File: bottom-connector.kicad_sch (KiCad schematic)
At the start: 6 parts, among them J1 Compute-Module-4_Plug_Connect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, Q3 DZDH0401DW, Q9 AO3401A

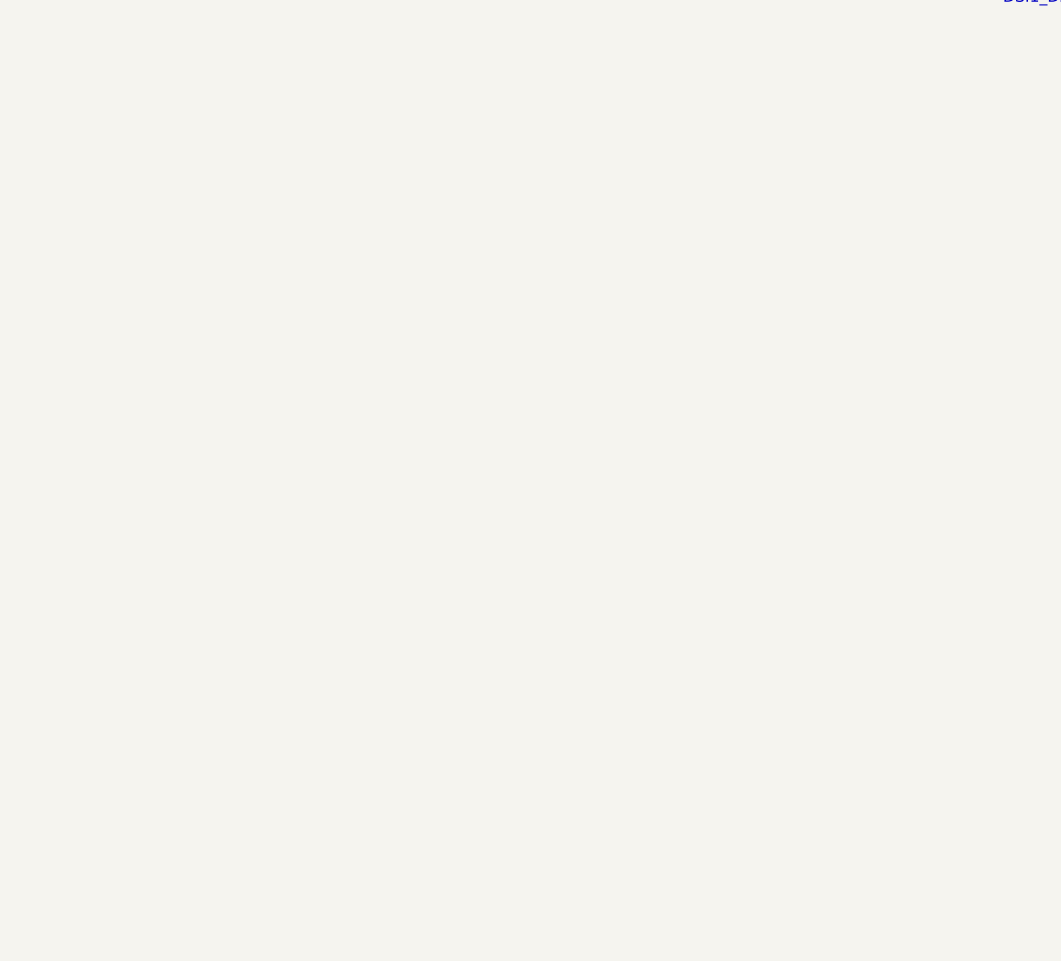
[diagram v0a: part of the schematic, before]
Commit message: [#57505] Continue migration to hierarchical schematic
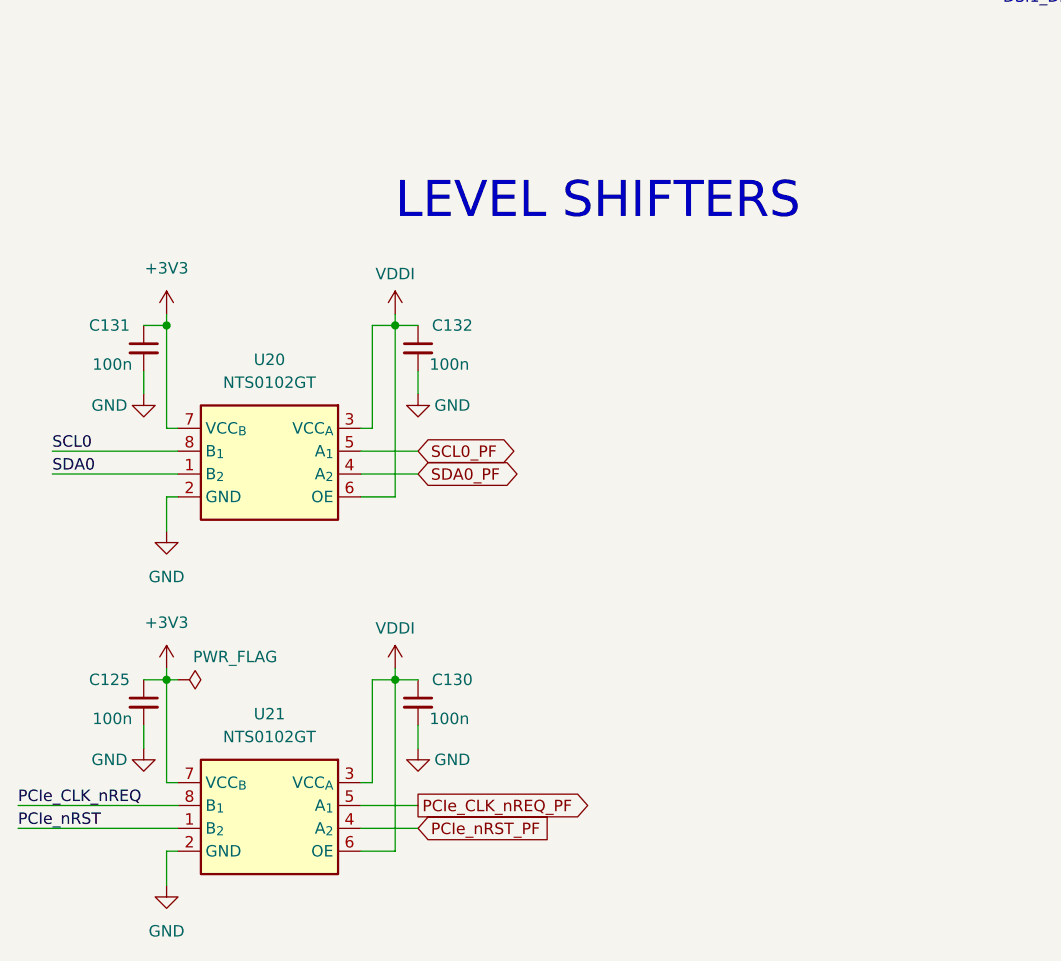
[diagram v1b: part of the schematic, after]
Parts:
- added C125, C130, C131, C132: C_100n_0402, antmicro-footprints:C_0402_1005Metric, symbol antmicroCapacitors0402:C_100n_0402
- added U20, U21: NTS0102_XSON, antmicro-footprints:XSON-8_1x1.95mm_P0.5mm, symbol antmicroLogicTranslatorsLevelShifters:NTS0102_XSON
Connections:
- net GND: now also C125.2, C130.2, C131.2, C132.2, U20.2 (GND), U21.2 (GND)
- net PCIe_CLK_nREQ: now also U21.8 (B_{1})
- net PCIe_nRST: now also U21.1 (B_{2})
- new net +3V3: C125.1, C131.1, U20.7 (VCC_{B}), U21.7 (VCC_{B})
- new net PCIe_CLK_nREQ_PF: U21.5 (A_{1})
- new net PCIe_nRST_PF: U21.4 (A_{2})
- new net SCL0: U20.8 (B_{1})
- new net SCL0_PF: U20.5 (A_{1})
- new net SDA0: U20.1 (B_{2})
- new net SDA0_PF: U20.4 (A_{2})
- new net VDDI: C130.1, C132.1, U20.3 (VCC_{A}), U20.6 (OE), U21.3 (VCC_{A}), U21.6 (OE)
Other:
- note added: "LEVEL SHIFTERS"

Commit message: [#57505] Finish defining buses
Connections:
- net CONN_USB_N renamed CONN.D_N
- net CONN_USB_P renamed CONN.D_P
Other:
- moved on the sheet: C125, C130, C131, C132, U20, U21

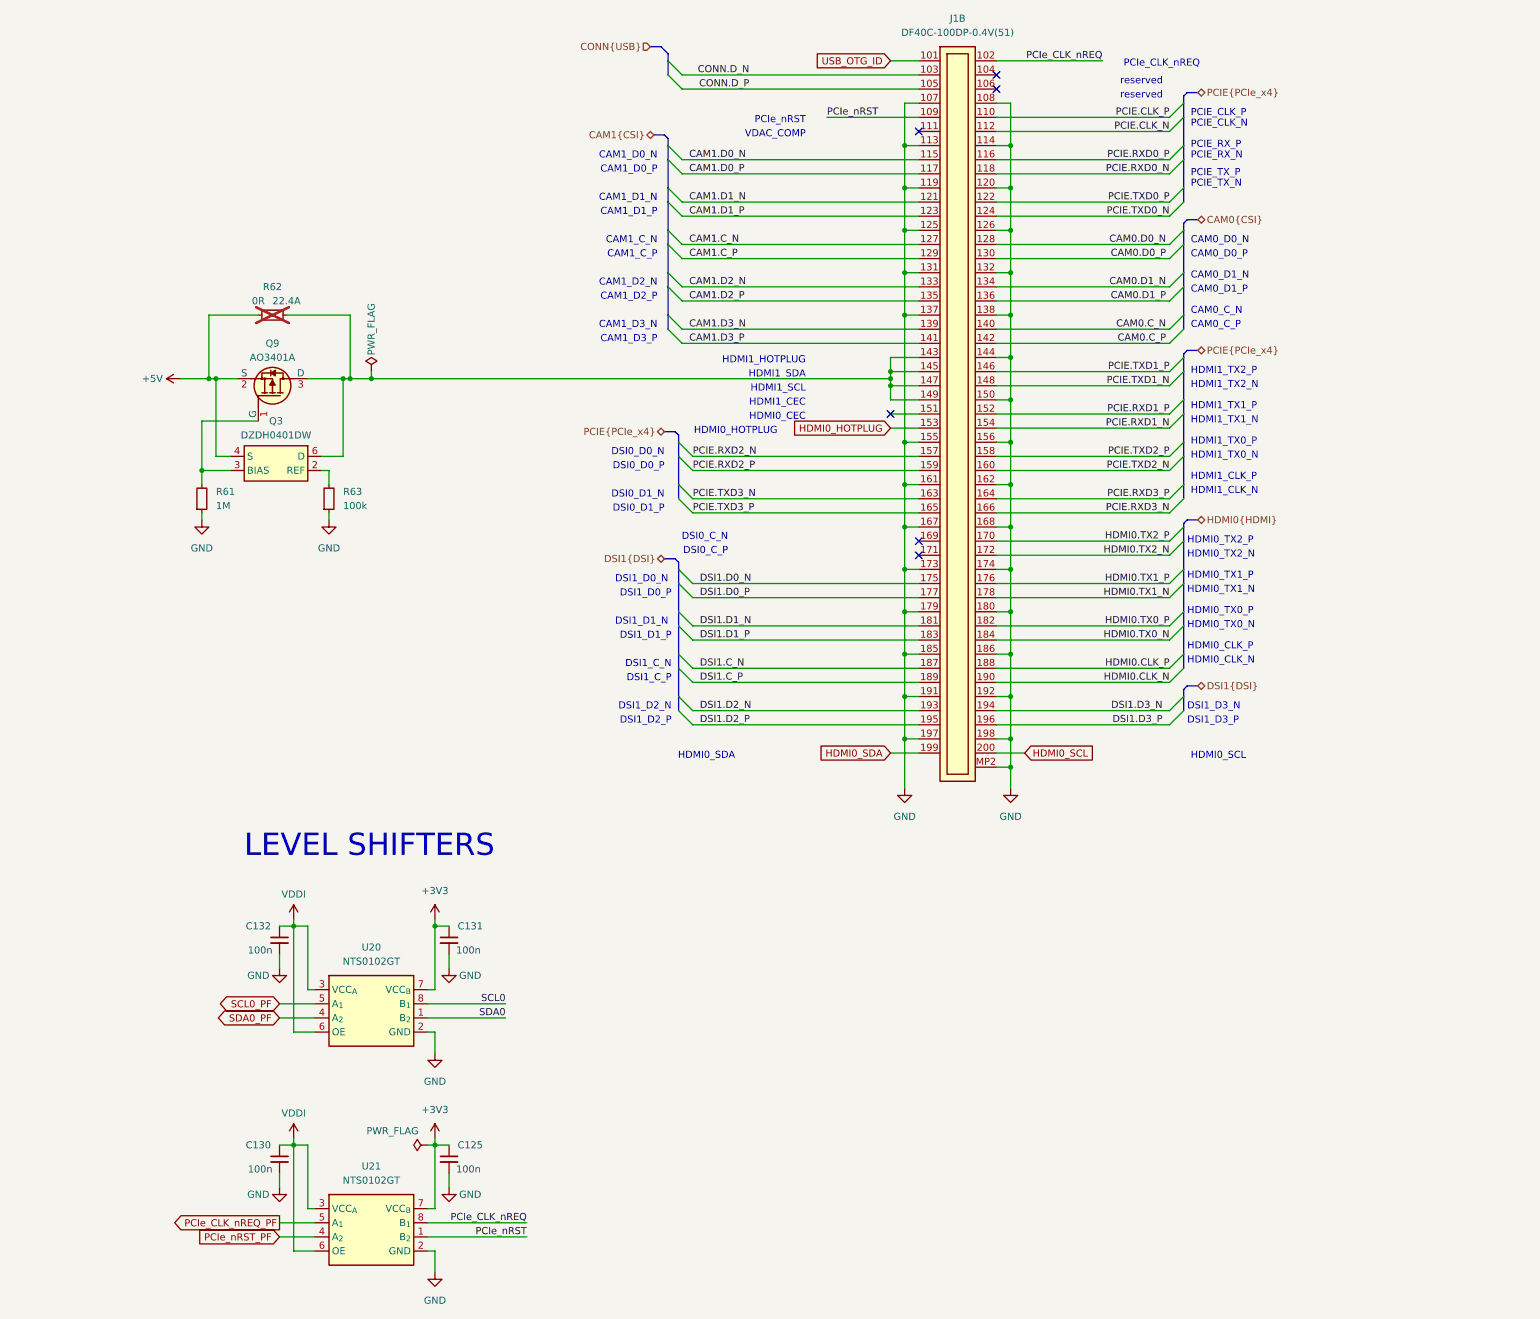
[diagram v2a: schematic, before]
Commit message: [#57505] Start moving logic level converters to GPIO sheet
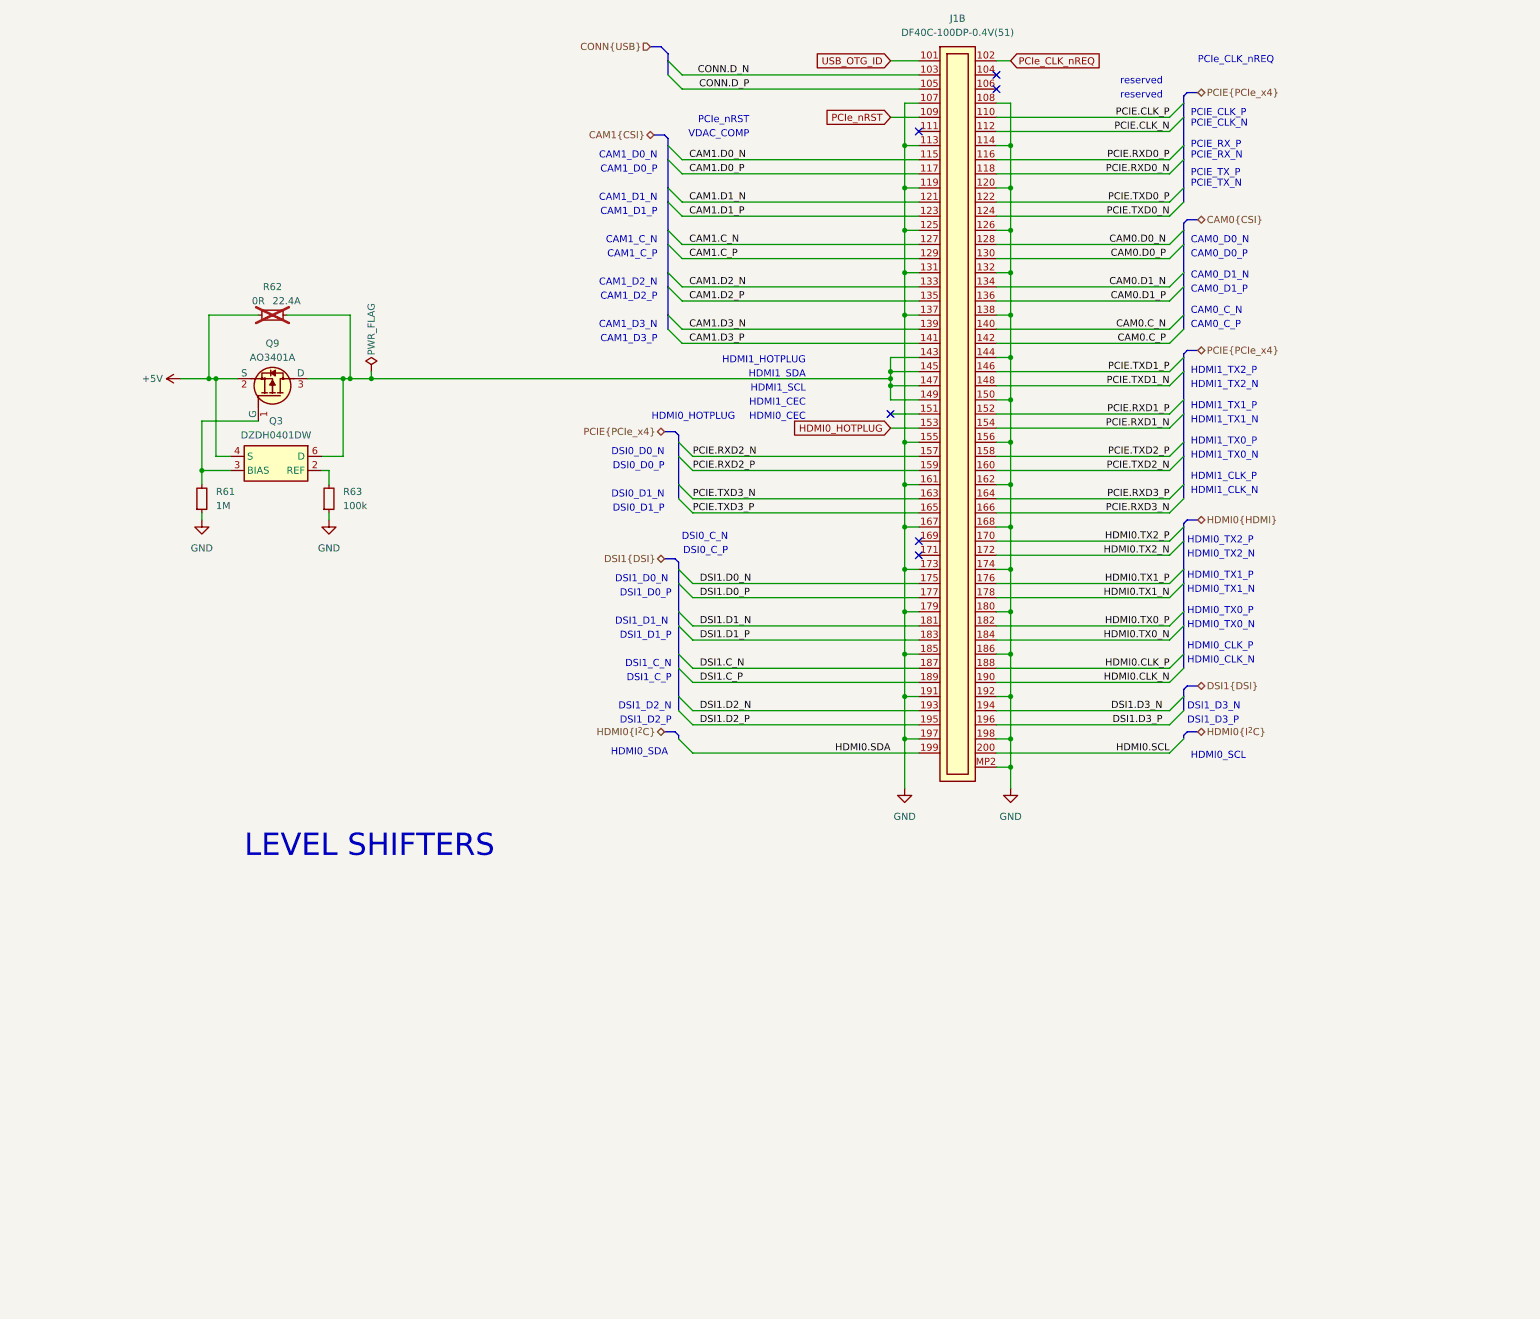
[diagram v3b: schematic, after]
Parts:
- removed C125, C130, C131, C132: C_100n_0402, antmicro-footprints:C_0402_1005Metric, symbol antmicroCapacitors0402:C_100n_0402
- removed U20, U21: NTS0102_XSON, antmicro-footprints:XSON-8_1x1.95mm_P0.5mm, symbol antmicroLogicTranslatorsLevelShifters:NTS0102_XSON
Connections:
- net HDMI0_SCL renamed HDMI0.SCL
- net HDMI0_SDA renamed HDMI0.SDA

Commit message: [#57422] Finishing touches
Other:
- note removed: "LEVEL SHIFTERS"
- moved on the sheet: J1B, Q3, Q9, R61, R62, R63

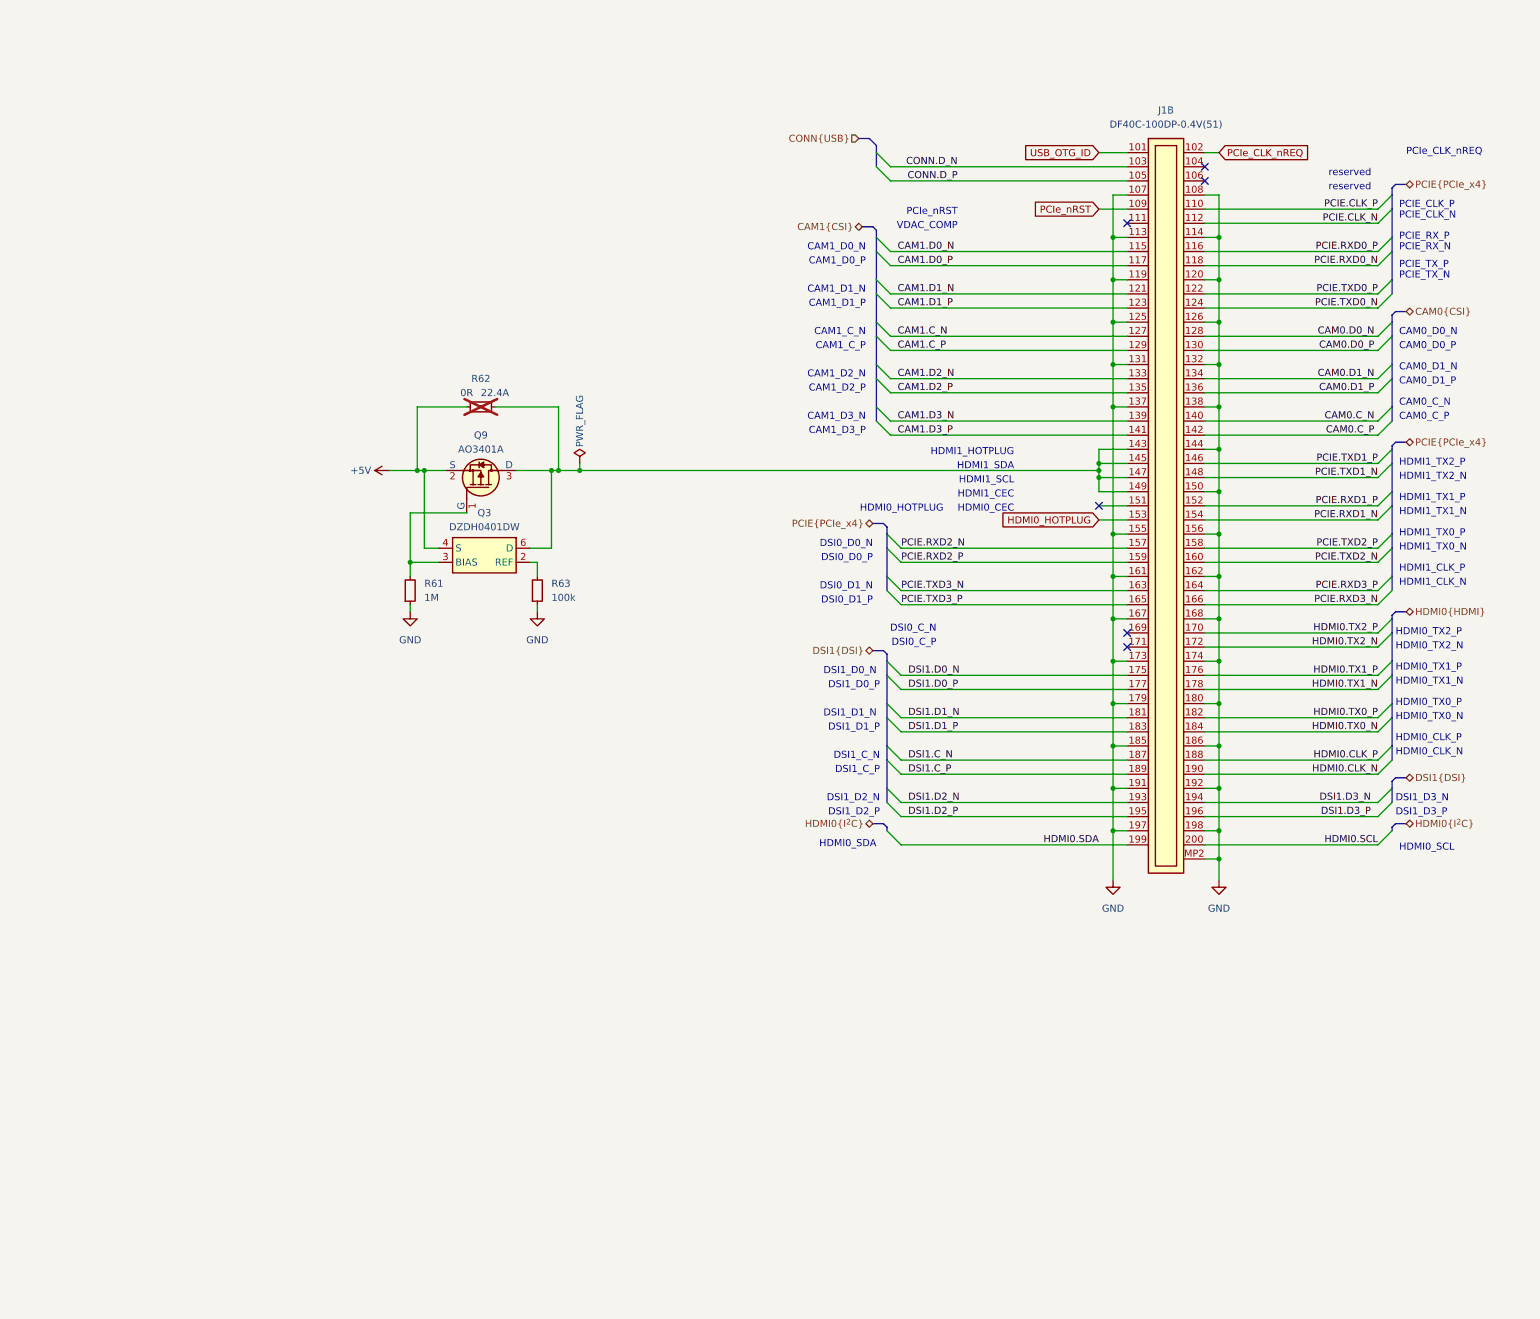
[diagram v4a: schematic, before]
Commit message: [#57422] Align schematics
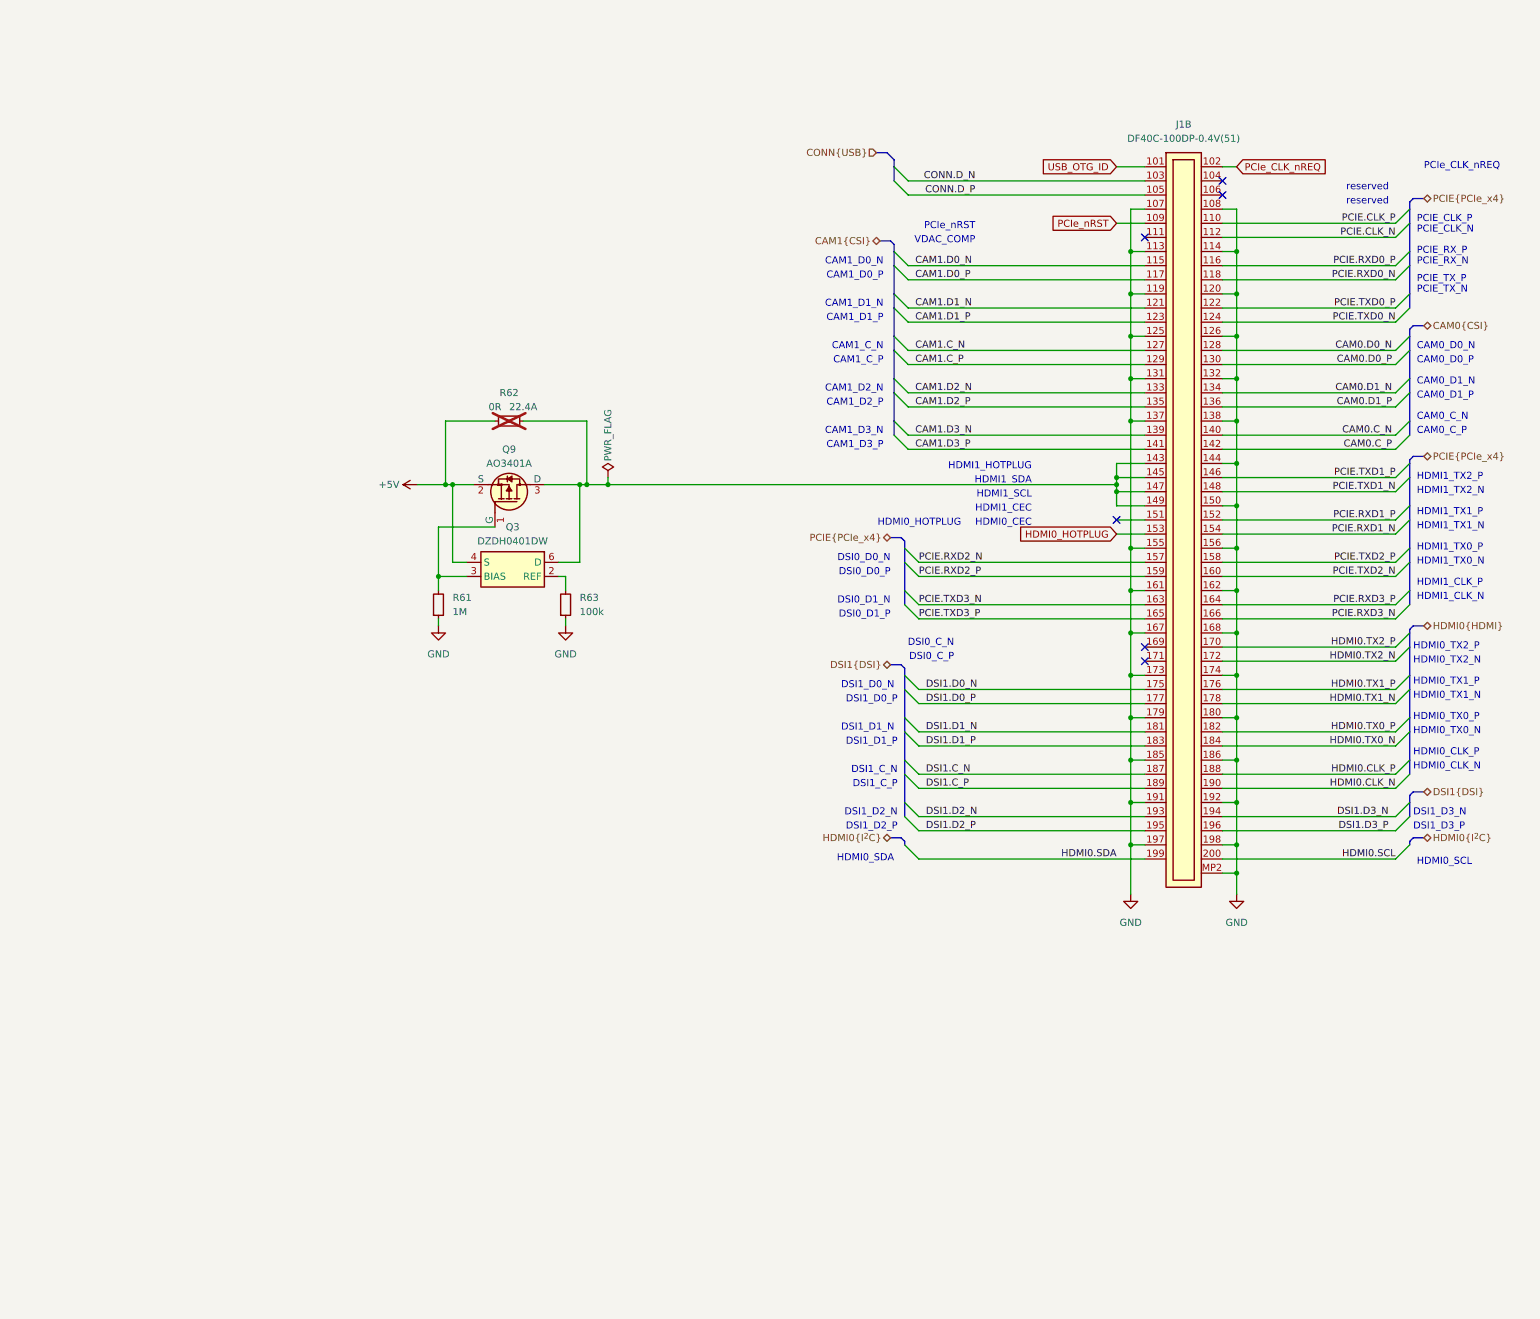
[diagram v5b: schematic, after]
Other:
- moved on the sheet: J1B, Q3, Q9, R61, R62, R63
